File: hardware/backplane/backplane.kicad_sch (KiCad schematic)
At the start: 31 parts, among them J1 Mgmt_Module, J10 Bus_PCI_Express_x1, J11 UPS_UART, J2 PWR, J3 Bus_PCI_Express_x1, J4 Bus_PCI_Express_x1, J5 Bus_PCI_Express_x1, J6 Bus_PCI_Express_x1, J7 Bus_PCI_Express_x1, J8 Bus_PCI_Express_x1, J9 Bus_PCI_Express_x1, M1 FAN1, M2 FAN2, M3 FAN3, M4 FAN4, U1 TPS5430DDA, U2 TCA9548APWR, U3 74HC4051

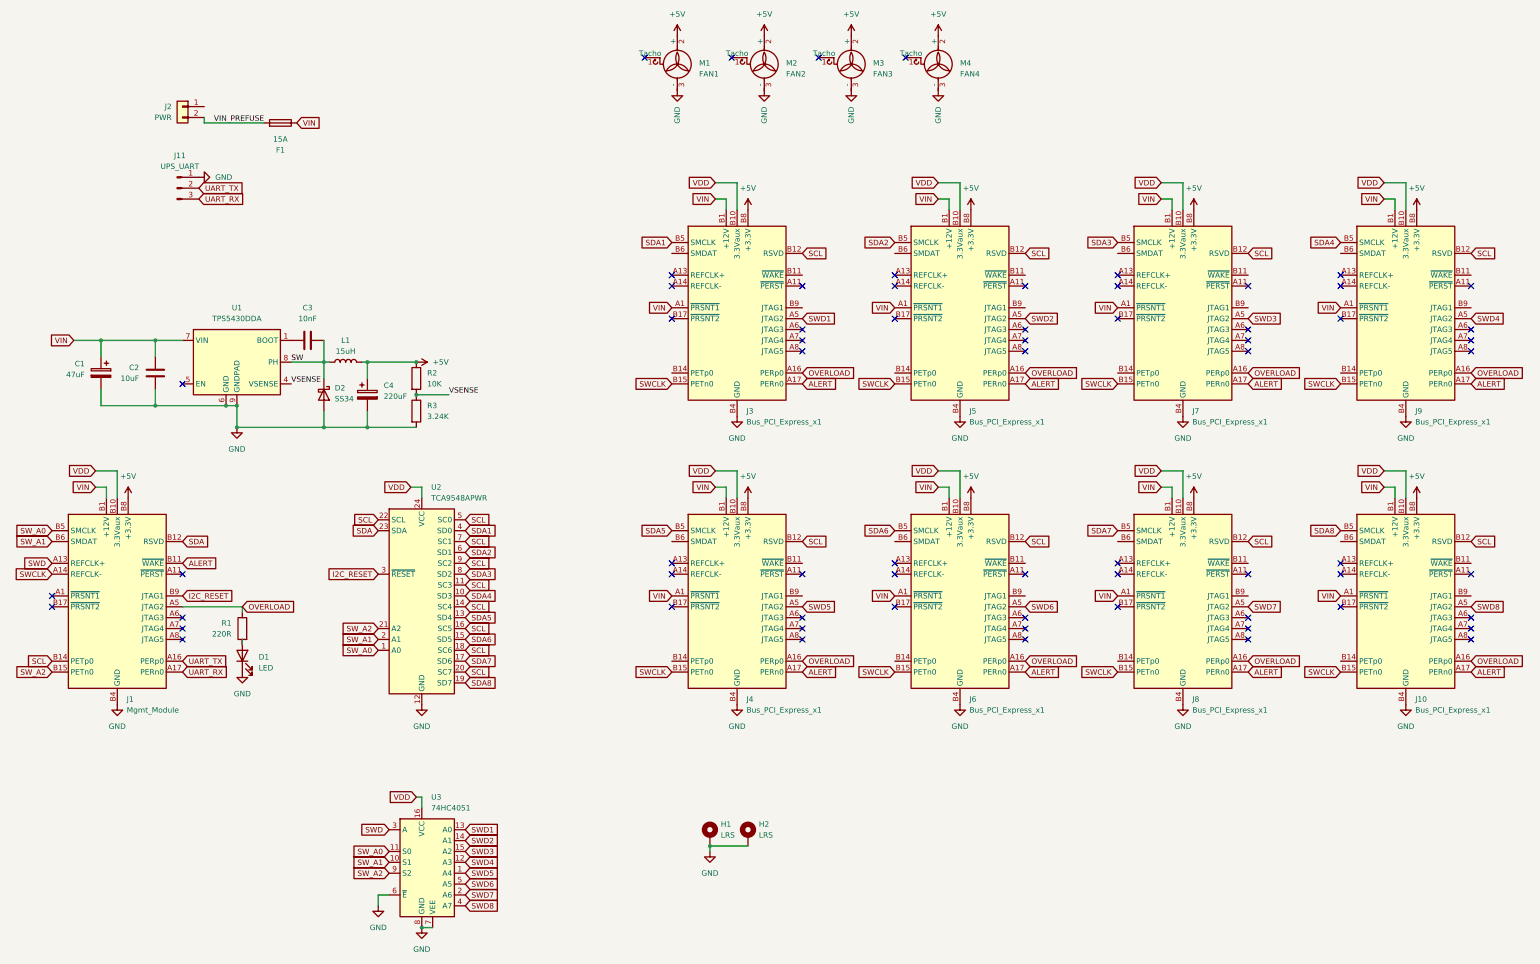
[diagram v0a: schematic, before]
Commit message: fix: add decoupling caps to i2c and swd switches
fix: add pullup resistor to i2c switch reset pin
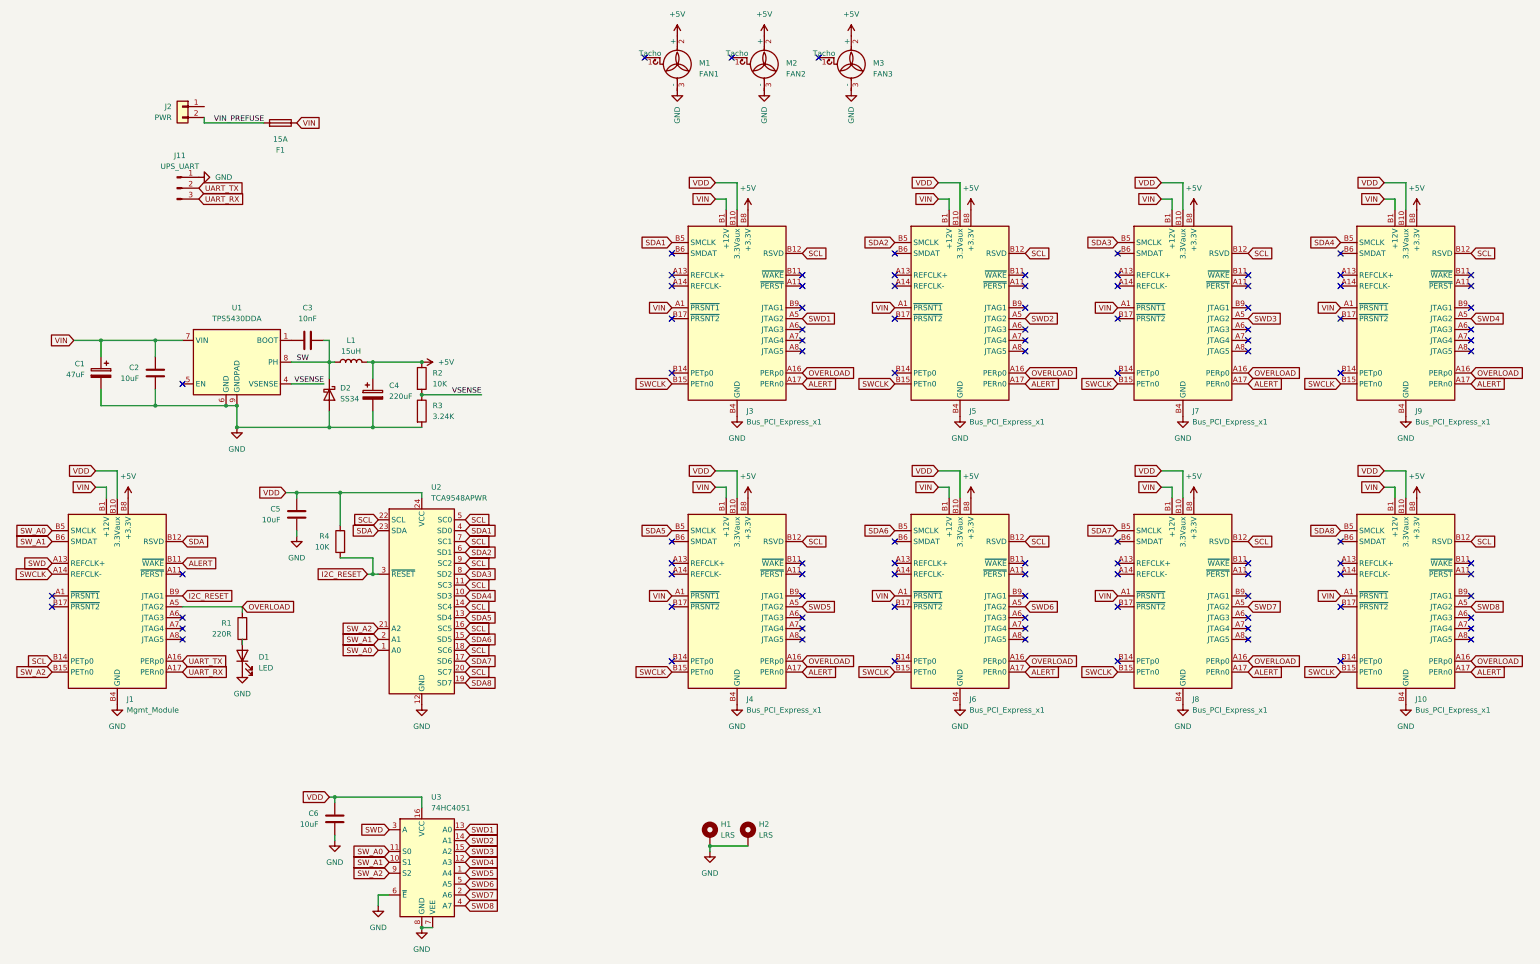
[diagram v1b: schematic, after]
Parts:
- removed M4: FAN4, Connector:FanPinHeader_1x03_P2.54mm_Vertical, symbol Motor:Fan_3pin
- added C5, C6: 10uF, Capacitor_SMD:C_0805_2012Metric, symbol Device:C
- added R4: 10K, Resistor_SMD:R_0603_1608Metric, symbol Device:R
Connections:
- net GND: now also C5.2, C6.2
- net I2C_RESET: now also R4.2
- net VDD: now also C5.1, C6.1, R4.1
- no-connect marks 67 -> 98
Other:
- moved on the sheet: C4, D2, L1, R2, R3

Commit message: chore: update pcb build config
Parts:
- J1, J10, J3, J4, J5, J6, J7, J8, J9: JLCPCB_CORRECTION (none) -> -2.1;0.05;0; LCSC (none) -> C404113; now in the parts list
- J11: JLCPCB_CORRECTION (none) -> 2.54;0;180; LCSC (none) -> C163036
- M1, M2, M3: JLCPCB_CORRECTION (none) -> 2.54;0;0; LCSC (none) -> C86503
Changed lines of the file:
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@@
 		(unit 1)
 		(exclude_from_sim no)
-		(in_bom no)
+		(in_bom yes)
 		(on_board yes)
 		(dnp no)
@@
 			)
 		)
-		(property "LCSC" ""
+		(property "LCSC" "C404113"
 			(at 207.01 99.06 0)
 			(effects
@@
 			)
 		)
+		(property "JLCPCB_CORRECTION" "-2.1;0.05;0"
+			(at 207.01 99.06 0)
+			(effects
+				(font
+					(size 1.27 1.27)
+				)
+				(hide yes)
+			)
+		)
 		(pin "A10"
 		)
@@
 		(unit 1)
 		(exclude_from_sim no)
-		(in_bom no)
+		(in_bom yes)
 		(on_board yes)
 		(dnp no)
@@
 			)
 		)
-		(property "LCSC" ""
+		(property "LCSC" "C404113"
 			(at 259.08 99.06 0)
 			(effects
@@
 			)
 		)
+		(property "JLCPCB_CORRECTION" "-2.1;0.05;0"
+			(at 259.08 99.06 0)
+			(effects
+				(font
+					(size 1.27 1.27)
+				)
+				(hide yes)
+			)
+		)
 		(pin "A10"
 		)
@@
 			)
 		)
+		(property "LCSC" "C163036"
+			(at 76.2 68.58 0)
+			(effects
+				(font
+					(size 1.27 1.27)
+				)
+				(hide yes)
+			)
+		)
+		(property "JLCPCB_CORRECTION" "2.54;0;180"
+			(at 76.2 68.58 0)
+			(effects
+				(font
+					(size 1.27 1.27)
+				)
+				(hide yes)
+			)
+		)
 		(pin "1"
 		)
@@
 		(unit 1)
 		(exclude_from_sim no)
-		(in_bom no)
+		(in_bom yes)
 		(on_board yes)
 		(dnp no)
@@
 			)
 		)
-		(property "LCSC" ""
+		(property "LCSC" "C404113"
 			(at 207.01 166.37 0)
 			(effects
@@
 			)
 		)
+		(property "JLCPCB_CORRECTION" "-2.1;0.05;0"
+			(at 207.01 166.37 0)
+			(effects
+				(font
+					(size 1.27 1.27)
+				)
+				(hide yes)
+			)
+		)
 		(pin "A10"
 		)
@@
 			)
 		)
+		(property "LCSC" "C86503"
+			(at 193.04 38.1 0)
+			(effects
+				(font
+					(size 1.27 1.27)
+				)
+				(hide yes)
+			)
+		)
+		(property "JLCPCB_CORRECTION" "2.54;0;0"
+			(at 193.04 38.1 0)
+			(effects
+				(font
+					(size 1.27 1.27)
+				)
+				(hide yes)
+			)
+		)
 		(pin "2"
 		)
@@
 		(unit 1)
 		(exclude_from_sim no)
-		(in_bom no)
+		(in_bom yes)
 		(on_board yes)
 		(dnp no)
@@
 			)
 		)
-		(property "LCSC" ""
+		(property "LCSC" "C404113"
 			(at 259.08 166.37 0)
 			(effects
@@
 			)
 		)
+		(property "JLCPCB_CORRECTION" "-2.1;0.05;0"
+			(at 259.08 166.37 0)
+			(effects
+				(font
+					(size 1.27 1.27)
+				)
+				(hide yes)
+			)
+		)
 		(pin "A10"
 		)
@@
 		(unit 1)
 		(exclude_from_sim no)
-		(in_bom no)
+		(in_bom yes)
 		(on_board yes)
 		(dnp no)
@@
 			)
 		)
-		(property "LCSC" ""
+		(property "LCSC" "C404113"
 			(at 311.15 166.37 0)
 			(effects
@@
 			)
 		)
+		(property "JLCPCB_CORRECTION" "-2.1;0.05;0"
+			(at 311.15 166.37 0)
+			(effects
+				(font
+					(size 1.27 1.27)
+				)
+				(hide yes)
+			)
+		)
 		(pin "A10"
 		)
@@
 			)
 		)
+		(property "LCSC" "C86503"
+			(at 233.68 38.1 0)
+			(effects
+				(font
+					(size 1.27 1.27)
+				)
+				(hide yes)
+			)
+		)
+		(property "JLCPCB_CORRECTION" "2.54;0;0"
+			(at 233.68 38.1 0)
+			(effects
+				(font
+					(size 1.27 1.27)
+				)
+				(hide yes)
+			)
+		)
 		(pin "2"
 		)
@@
 		(unit 1)
 		(exclude_from_sim no)
-		(in_bom no)
+		(in_bom yes)
 		(on_board yes)
 		(dnp no)
@@
 			)
 		)
-		(property "LCSC" ""
+		(property "LCSC" "C404113"
 			(at 62.23 166.37 0)
 			(effects
@@
 			)
 		)
+		(property "JLCPCB_CORRECTION" "-2.1;0.05;0"
+			(at 62.23 166.37 0)
+			(effects
+				(font
+					(size 1.27 1.27)
+				)
+				(hide yes)
+			)
+		)
 		(pin "A10"
 		)
@@
 		(unit 1)
 		(exclude_from_sim no)
-		(in_bom no)
+		(in_bom yes)
 		(on_board yes)
 		(dnp no)
@@
 			)
 		)
-		(property "LCSC" ""
+		(property "LCSC" "C404113"
 			(at 363.22 99.06 0)
 			(effects
@@
 			)
 		)
+		(property "JLCPCB_CORRECTION" "-2.1;0.05;0"
+			(at 363.22 99.06 0)
+			(effects
+				(font
+					(size 1.27 1.27)
+				)
+				(hide yes)
+			)
+		)
 		(pin "A10"
 		)
@@
 			)
 		)
+		(property "LCSC" "C86503"
+			(at 213.36 38.1 0)
+			(effects
+				(font
+					(size 1.27 1.27)
+				)
+				(hide yes)
+			)
+		)
+		(property "JLCPCB_CORRECTION" "2.54;0;0"
+			(at 213.36 38.1 0)
+			(effects
+				(font
+					(size 1.27 1.27)
+				)
+				(hide yes)
+			)
+		)
 		(pin "2"
 		)
@@
 		(unit 1)
 		(exclude_from_sim no)
-		(in_bom no)
+		(in_bom yes)
 		(on_board yes)
 		(dnp no)
@@
 			)
 		)
-		(property "LCSC" ""
+		(property "LCSC" "C404113"
 			(at 363.22 166.37 0)
 			(effects
@@
 			)
 		)
+		(property "JLCPCB_CORRECTION" "-2.1;0.05;0"
+			(at 363.22 166.37 0)
+			(effects
+				(font
+					(size 1.27 1.27)
+				)
+				(hide yes)
+			)
+		)
 		(pin "A10"
 		)
@@
 		(unit 1)
 		(exclude_from_sim no)
-		(in_bom no)
+		(in_bom yes)
 		(on_board yes)
 		(dnp no)
@@
 			)
 		)
-		(property "LCSC" ""
+		(property "LCSC" "C404113"
 			(at 311.15 99.06 0)
 			(effects
@@
 			(at 311.15 99.06 0)
 			(effects
+				(font
+					(size 1.27 1.27)
+				)
+				(hide yes)
+			)
+		)
+		(property "JLCPCB_CORRECTION" "-2.1;0.05;0"
+			(at 311.15 99.06 0)
+			(effects

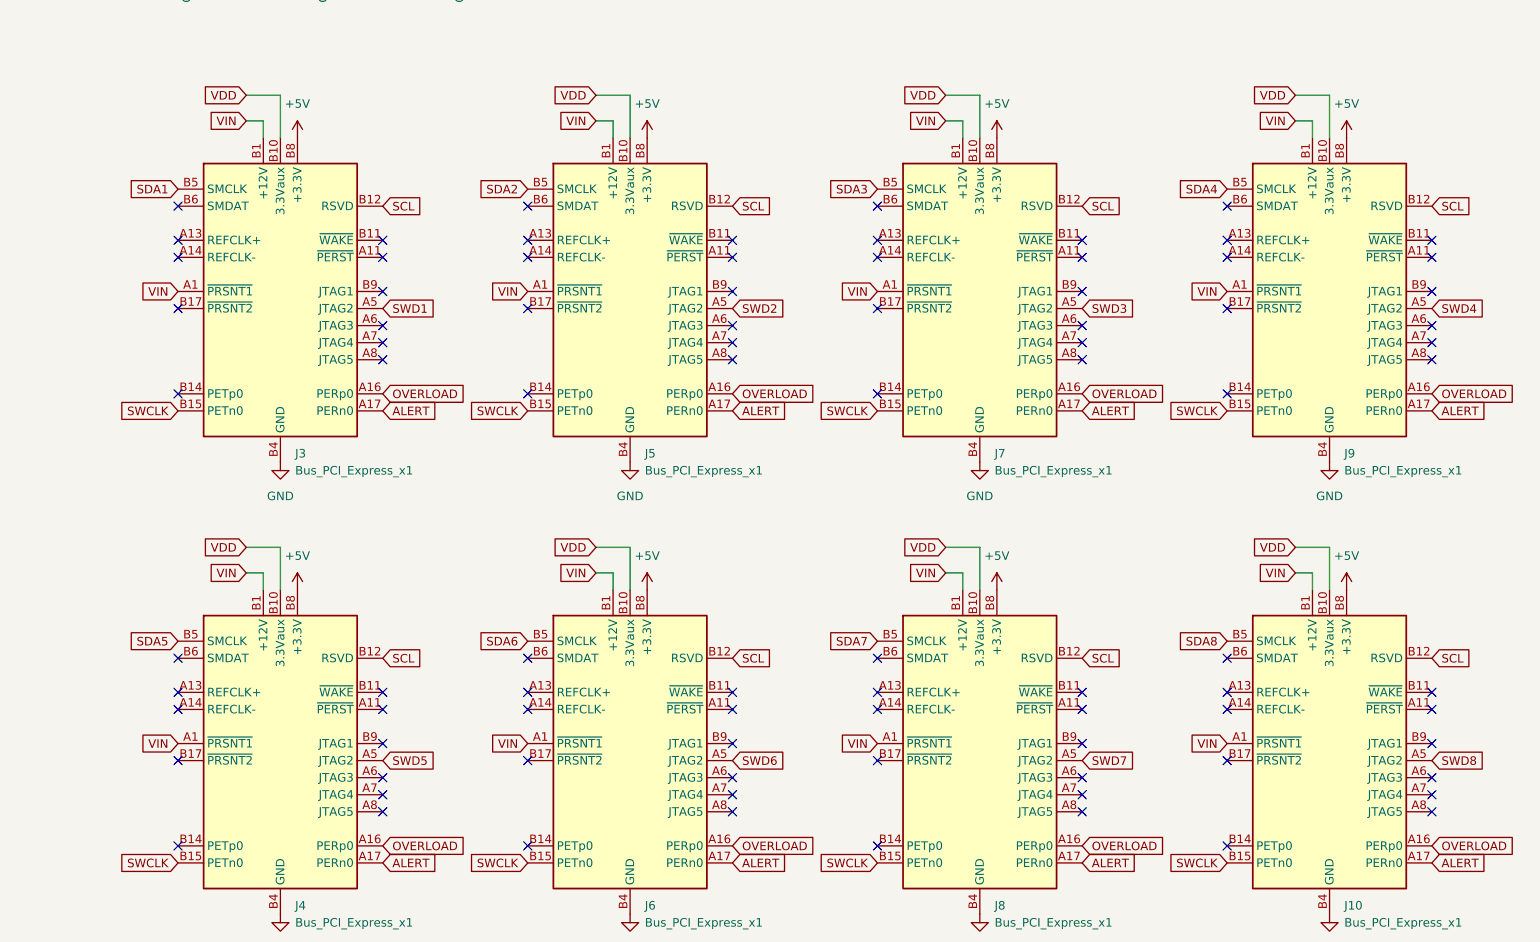
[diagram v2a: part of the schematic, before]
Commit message: feat: give vin 8 pins
fix: correct i2c pin mismatch
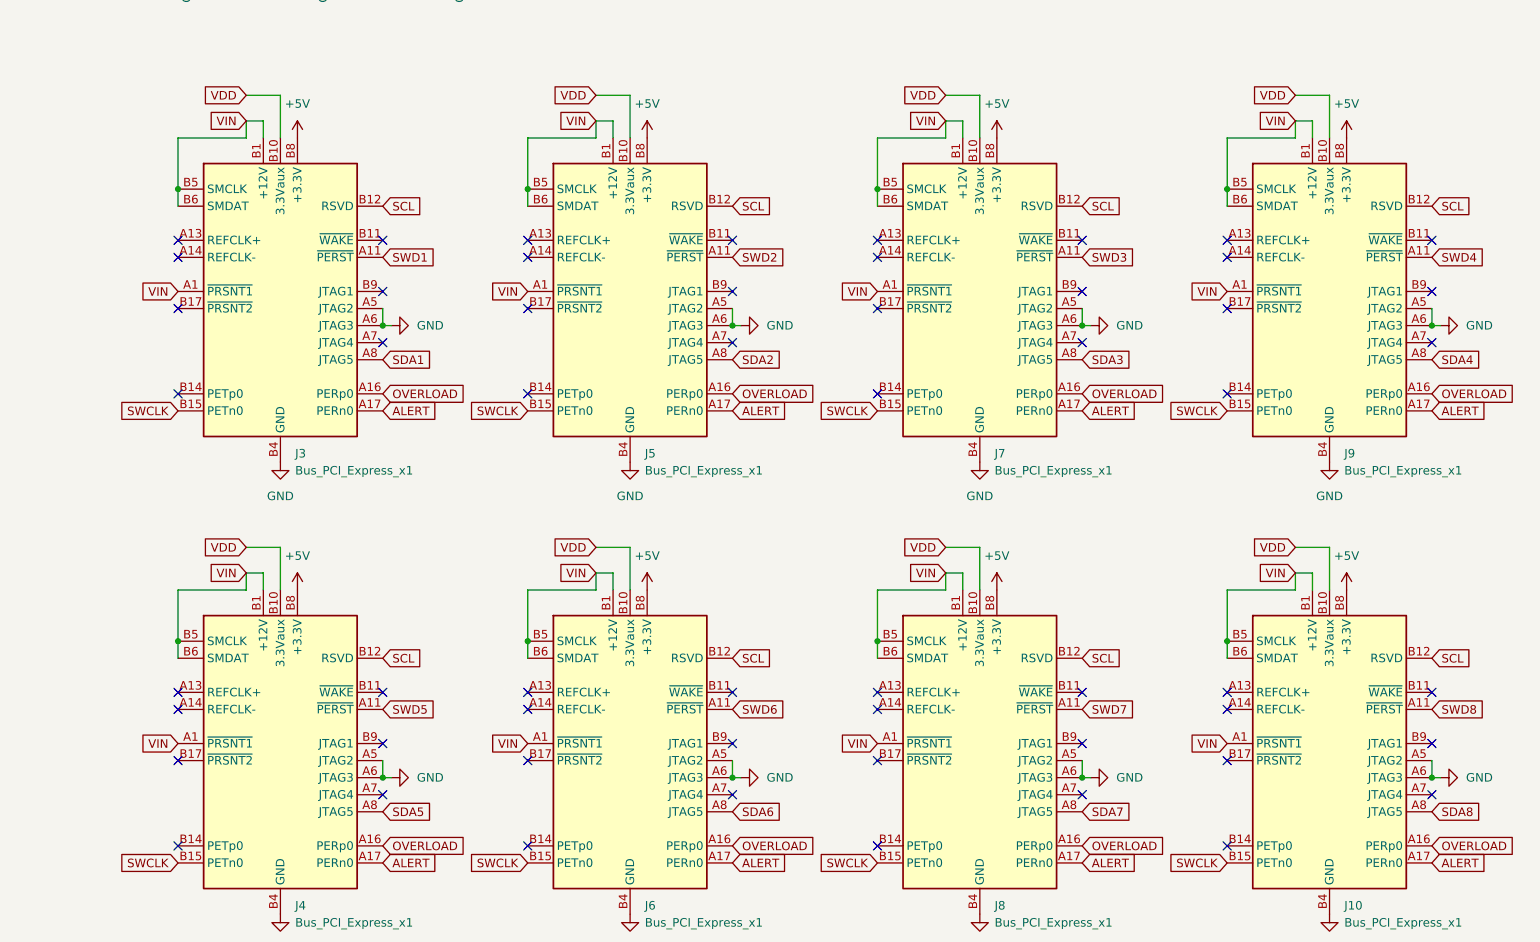
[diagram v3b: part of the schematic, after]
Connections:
- net GND: now also J10.A5 (JTAG2), J10.A6 (JTAG3), J3.A5 (JTAG2), J3.A6 (JTAG3), J4.A5 (JTAG2), J4.A6 (JTAG3), J5.A5 (JTAG2), J5.A6 (JTAG3), J6.A5 (JTAG2), J6.A6 (JTAG3), J7.A5 (JTAG2), J7.A6 (JTAG3), J8.A5 (JTAG2), J8.A6 (JTAG3), J9.A5 (JTAG2), J9.A6 (JTAG3)
- net SDA1: now also J3.A8 (JTAG5); no longer J3.B5 (SMCLK)
- net SDA2: now also J5.A8 (JTAG5); no longer J5.B5 (SMCLK)
- net SDA3: now also J7.A8 (JTAG5); no longer J7.B5 (SMCLK)
- net SDA4: now also J9.A8 (JTAG5); no longer J9.B5 (SMCLK)
- net SDA5: now also J4.A8 (JTAG5); no longer J4.B5 (SMCLK)
- net SDA6: now also J6.A8 (JTAG5); no longer J6.B5 (SMCLK)
- net SDA7: now also J8.A8 (JTAG5); no longer J8.B5 (SMCLK)
- net SDA8: now also J10.A8 (JTAG5); no longer J10.B5 (SMCLK)
- net SWD1: now also J3.A11 (~{PERST}); no longer J3.A5 (JTAG2)
- net SWD2: now also J5.A11 (~{PERST}); no longer J5.A5 (JTAG2)
- net SWD3: now also J7.A11 (~{PERST}); no longer J7.A5 (JTAG2)
- net SWD4: now also J9.A11 (~{PERST}); no longer J9.A5 (JTAG2)
- net SWD5: now also J4.A11 (~{PERST}); no longer J4.A5 (JTAG2)
- net SWD6: now also J6.A11 (~{PERST}); no longer J6.A5 (JTAG2)
- net SWD7: now also J8.A11 (~{PERST}); no longer J8.A5 (JTAG2)
- net SWD8: now also J10.A11 (~{PERST}); no longer J10.A5 (JTAG2)
- net VIN: now also J10.B5 (SMCLK), J10.B6 (SMDAT), J3.B5 (SMCLK), J3.B6 (SMDAT), J4.B5 (SMCLK), J4.B6 (SMDAT), J5.B5 (SMCLK), J5.B6 (SMDAT), J6.B5 (SMCLK), J6.B6 (SMDAT), J7.B5 (SMCLK), J7.B6 (SMDAT), J8.B5 (SMCLK), J8.B6 (SMDAT), J9.B5 (SMCLK), J9.B6 (SMDAT)
- no-connect marks 98 -> 66
